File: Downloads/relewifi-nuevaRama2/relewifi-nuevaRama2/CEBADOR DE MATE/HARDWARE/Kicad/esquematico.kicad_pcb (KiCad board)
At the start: 2 copper layers, 50 parts, among them J1 Screw_Terminal_01x02, J10 LCD I2C, J12 Screw_Terminal_01x02, J13 Screw_Terminal_01x02, J14 Screw_Terminal_01x02, J15 Screw_Terminal_01x02, J2 Screw_Terminal_01x02, J3 Screw_Terminal_01x02, J4 Screw_Terminal_01x02, J5 Screw_Terminal_01x02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

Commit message: se termino el pcb y ya lo ordene
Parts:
- moved U3 18.5 mm to (90.7, 91.2)
- moved C2 17.8 mm to (89.5, 99.1)
- moved C1 17.5 mm to (95.5, 95.5)
- moved J1 6.58 mm to (73.0, 90.0)
- moved U2 4.51 mm to (83.5, 131.0)
- moved J10 4.09 mm to (82.5, 161.5), turned to 180 degrees
- moved D5 3.01 mm to (128.0, 151.5), turned to 0 degrees
- moved U4 0.08 mm to (108.3, 90.4)
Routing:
- net +5V: track 3.92 -> 97.8 mm
- net 12V: track 133.1 -> 199.5 mm, vias 0 -> 1
- net SCL: track 0.00 -> 53.3 mm
- net SDA: track 1.40 -> 44.0 mm
- net GPIO17: track 0.00 -> 30.1 mm, vias 0 -> 1
- net GPIO18: track 2.72 -> 27.3 mm
- net 5V: track 0.00 -> 21.1 mm
- net Net-(Q3-G): track 6.16 -> 17.5 mm
- net Net-(D5-A): track 0.00 -> 10.2 mm
- net Net-(D2-A): track 4.50 -> 14.6 mm
- net GPIO19: track 3.43 -> 13.5 mm
- net GPIO23: track 10.5 -> 18.9 mm
- net Net-(D7-A): track 0.24 -> 8.43 mm
- net Net-(Q4-G): track 5.77 -> 13.5 mm
- net Net-(D6-A): track 0.00 -> 7.71 mm
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- added copper zone on B.Cu, net GND
- added copper zone on F.Cu, net GND

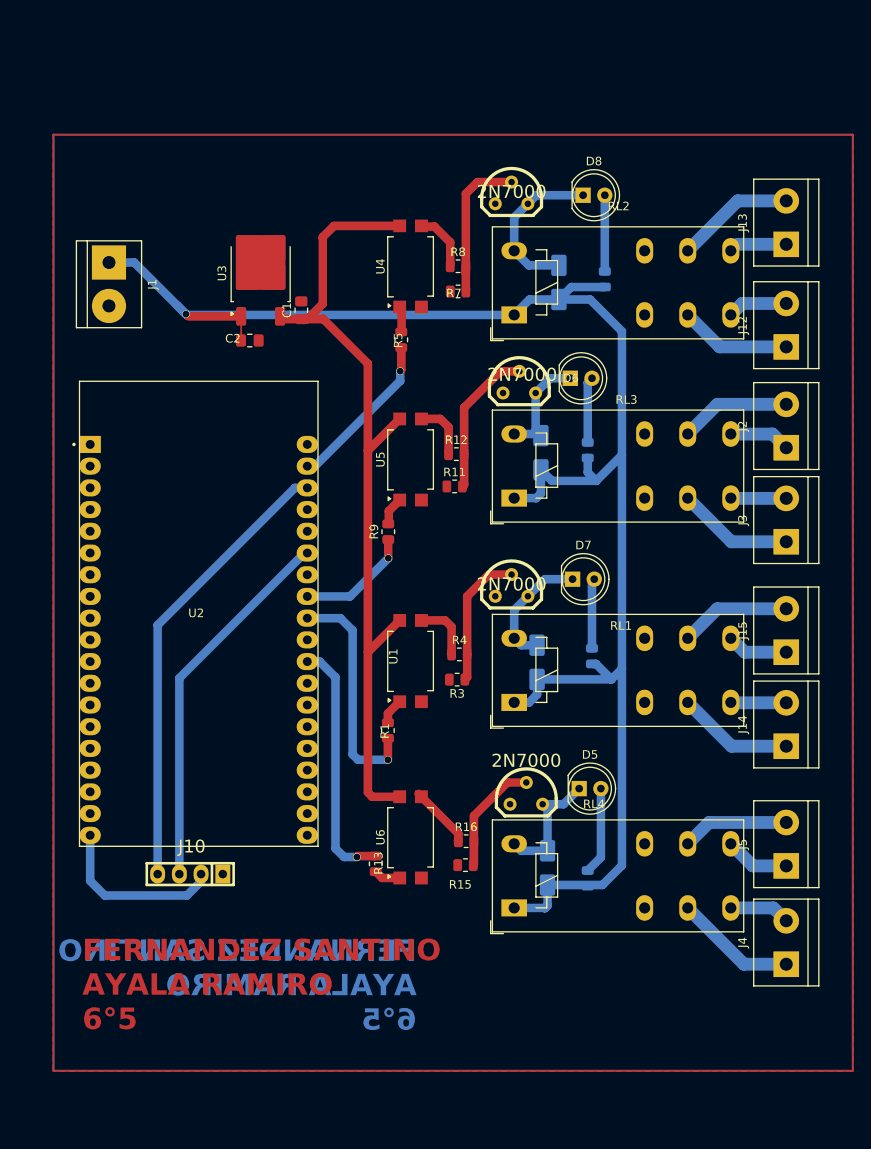
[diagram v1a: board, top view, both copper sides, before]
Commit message: termine el pcb y agregue una pinera para sensores,y agrande los pads y vias
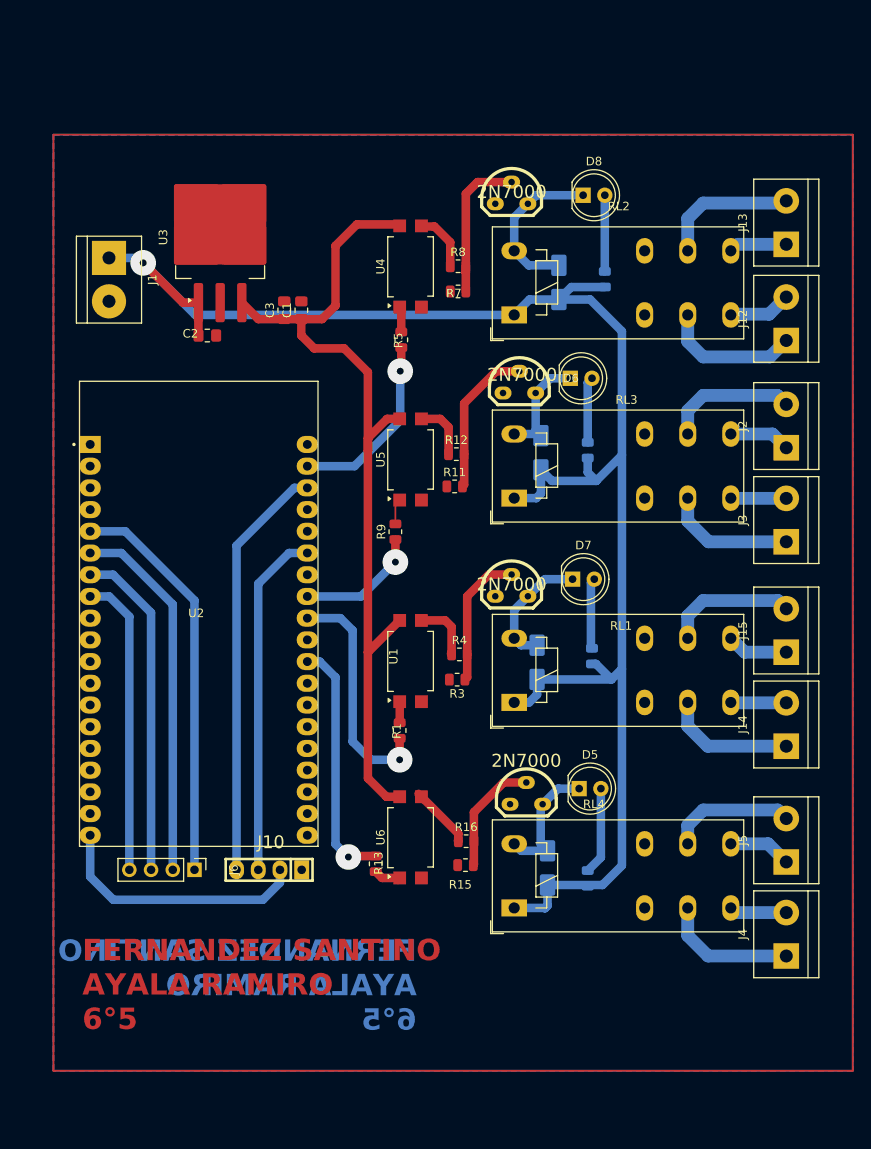
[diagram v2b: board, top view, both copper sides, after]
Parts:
- added C3: 0.1uf, Capacitor_SMD:C_0805_2012Metric_Pad1.18x1.45mm_HandSolder, F.Cu at (93.5, 95.5)
- added J6: PINERA, Connector_PinHeader_2.54mm:PinHeader_1x04_P2.54mm_Vertical, F.Cu at (83.0, 161.0)
- U3: footprint Package_TO_SOT_SMD:TO-252-2 -> Package_TO_SOT_SMD:TO-263-3_TabPin2
- moved J10 9.24 mm to (91.7, 161.0)
- moved U3 6.35 mm to (86.0, 87.0)
- moved C2 5.01 mm to (84.5, 98.5)
- moved R1 1.38 mm to (107.0, 144.7)
- moved J4 0.96 mm to (152.2, 171.1)
- moved R9 0.83 mm to (106.5, 121.5)
- moved J12 0.75 mm to (152.2, 99.1)
- moved J1 0.54 mm to (73.0, 89.4)
- moved J5 0.46 mm to (152.2, 160.1)
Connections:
- U2 pad J2-5: unconnected-(U2-IO34-PadJ2-5) -> GPIO34
- U2 pad J2-6: unconnected-(U2-IO35-PadJ2-6) -> GPIO35
- U2 pad J2-7: unconnected-(U2-IO32-PadJ2-7) -> GPIO32
- U2 pad J2-8: unconnected-(U2-IO33-PadJ2-8) -> GPIO33
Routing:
- net GPIO34: track 0.00 -> 47.1 mm
- net GPIO35: track 0.00 -> 43.2 mm
- net GPIO32: track 0.00 -> 39.0 mm
- net GPIO33: track 0.00 -> 35.2 mm
- net 5V: track 21.1 -> 30.5 mm
- net +5V: track 97.8 -> 103.0 mm
- net SCL: track 53.3 -> 49.0 mm
- net SDA: track 44.0 -> 40.7 mm
- net COM1: track 13.1 -> 16.2 mm
- net GPIO23: track 18.9 -> 21.7 mm
- net COM2.2: track 13.0 -> 15.4 mm
- net COM2.1: track 13.0 -> 15.3 mm
- net COM2.3: track 12.6 -> 14.8 mm
- net COM2: track 13.9 -> 16.2 mm
- net 12V: track 199.5 -> 201.1 mm
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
